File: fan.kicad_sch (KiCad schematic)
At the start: 10 parts, among them J6 Conn_01x04, U25 TMP1075NDRLR, U9 EMC2101

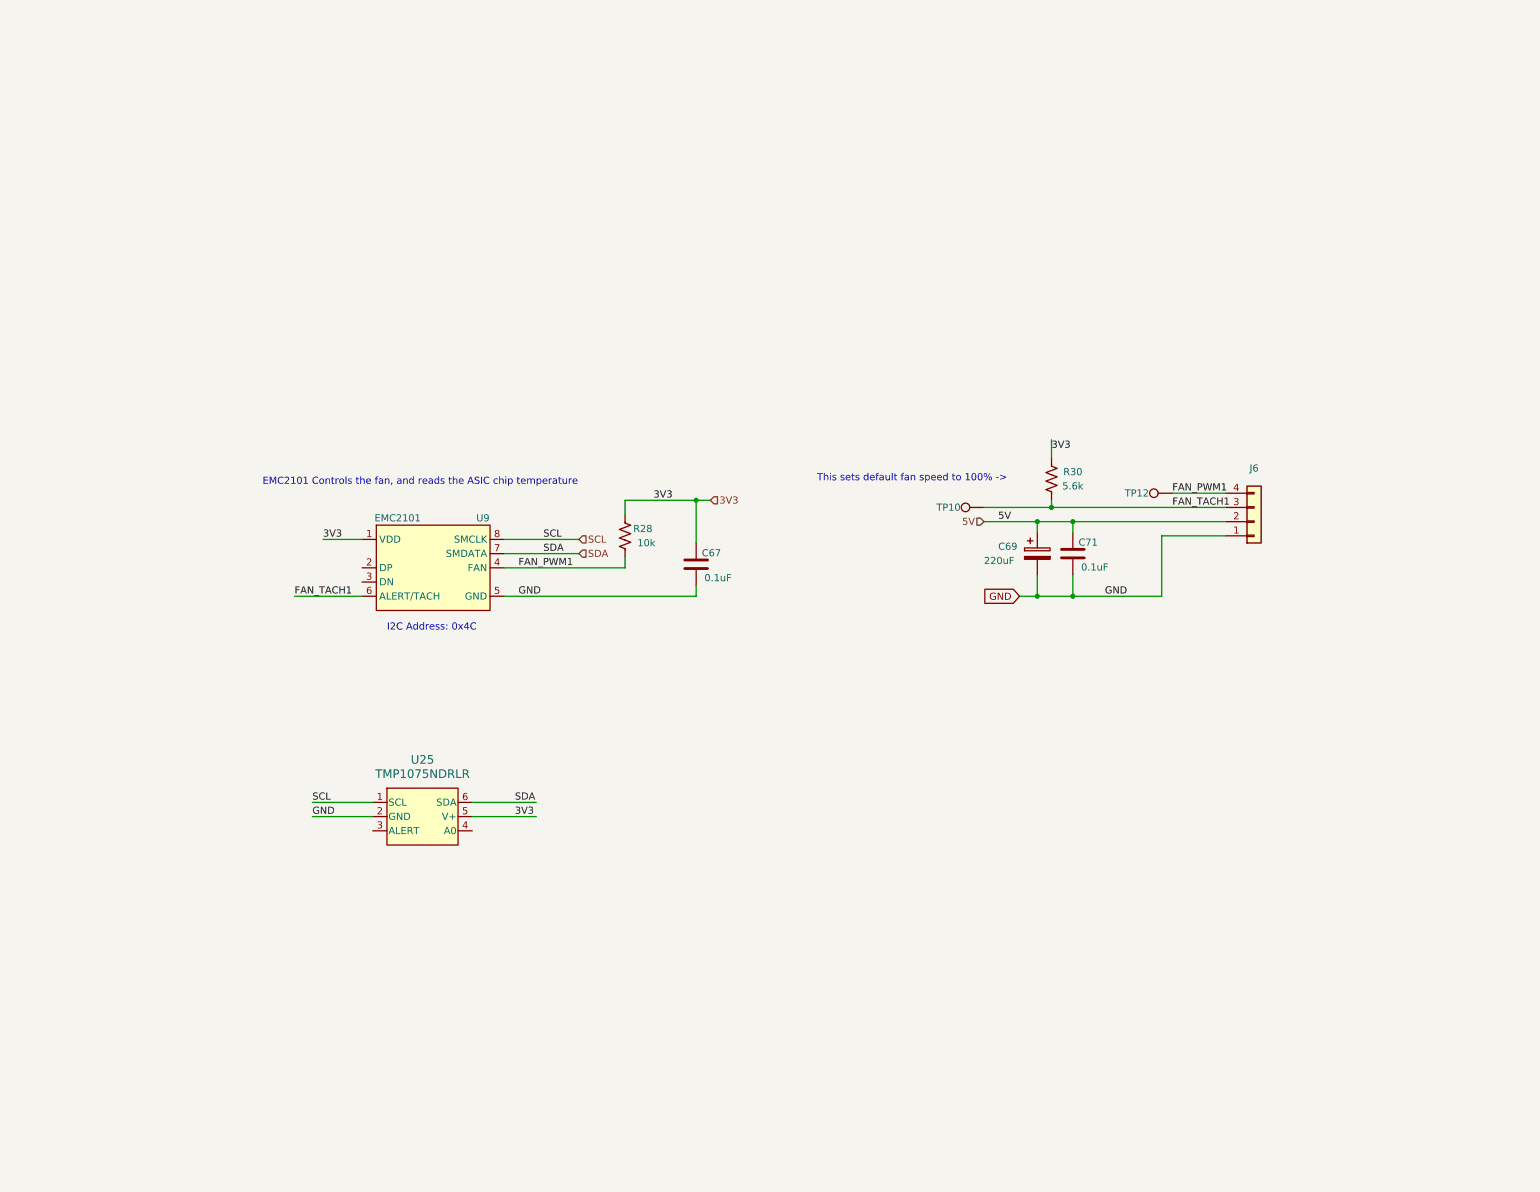
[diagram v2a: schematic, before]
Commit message: added EMC2302
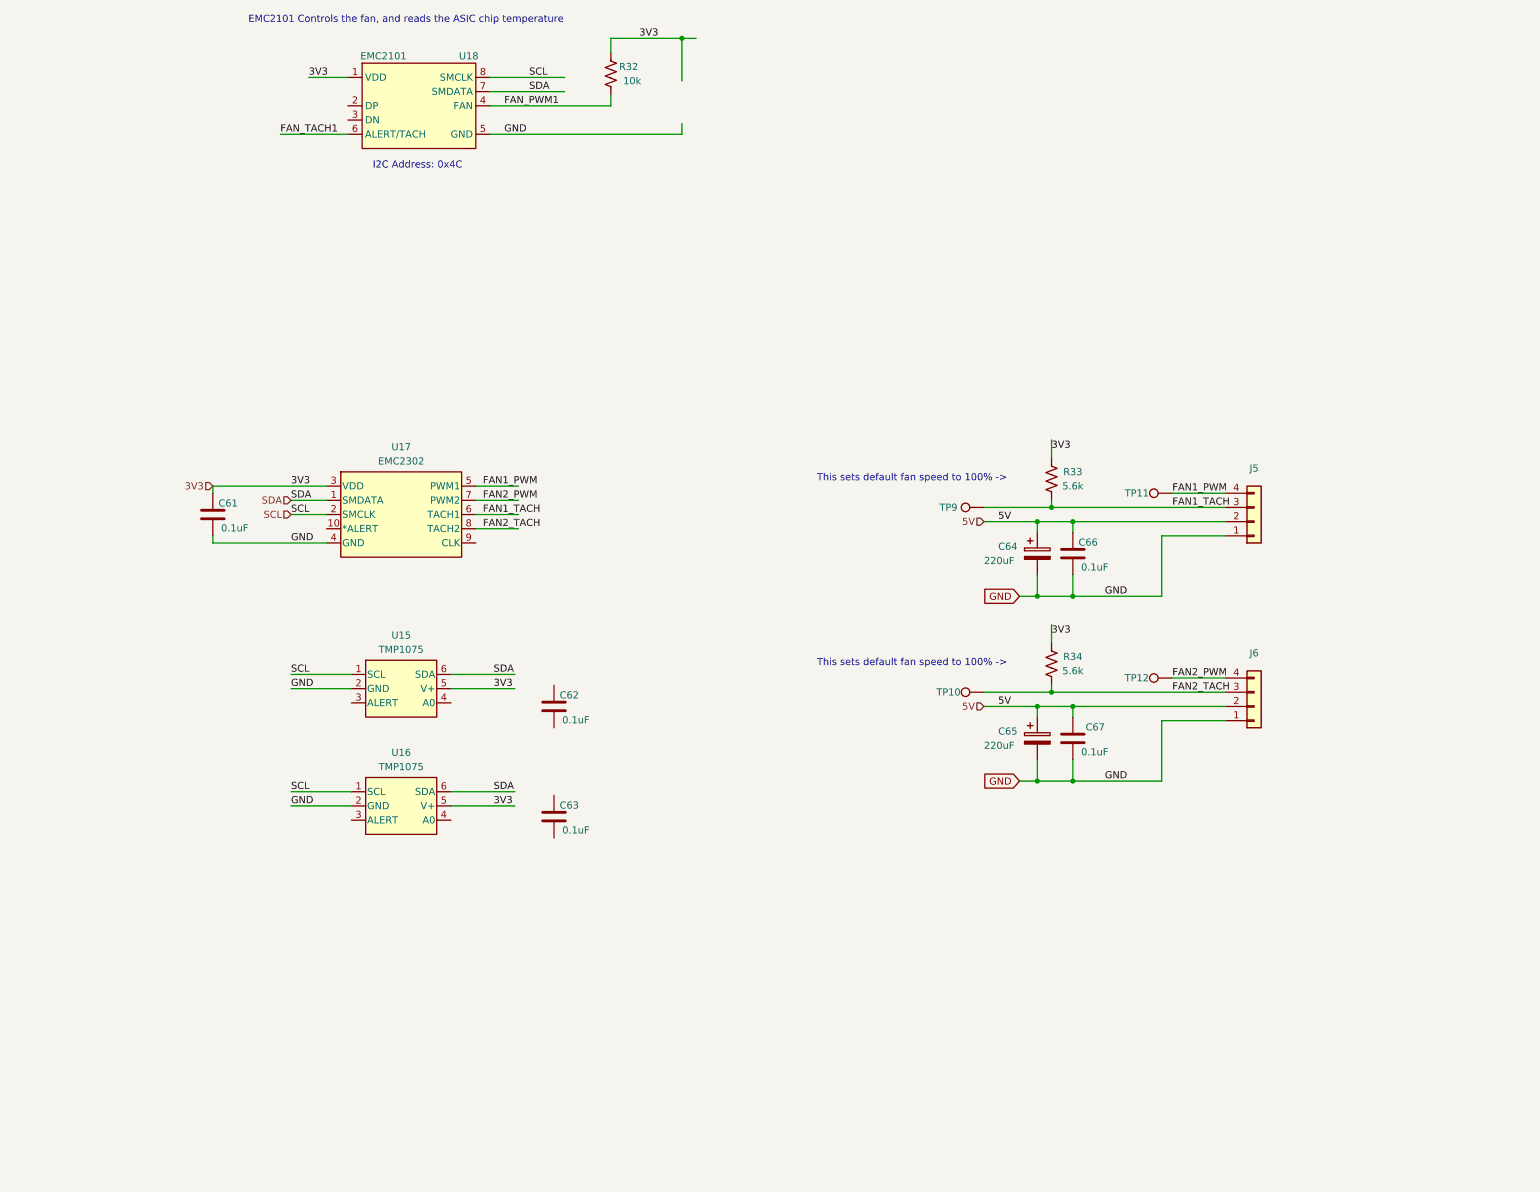
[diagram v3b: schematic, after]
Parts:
- added C62, C63, C67: 311-3342-1-ND, Capacitor_SMD:C_0402_1005Metric, symbol Device:C
- added C65: 220uF, Capacitor_SMD:CP_Elec_6.3x7.7, symbol Device:C_Polarized
- added J6: Conn_01x04, bitaxe:470531000, symbol Connector_Generic:Conn_01x04
- added R34: 5.6k, Resistor_SMD:R_0402_1005Metric, symbol Device:R_US
- added TP10, TP12: TestPoint, TestPoint:TestPoint_Pad_D1.5mm, symbol Connector:TestPoint
- added U16: TMP1075, bitaxe:SOT5X3-6_DRL_TEX, symbol bitaxe:TMP1075NDRLR
- added U17: EMC2302, MSOP10_MC_MCH, symbol bitaxe:EMC2302-2-AIZL-TR
- U15: renamed from U25; value TMP1075NDRLR -> TMP1075
- renumbered C67 to C61, C69 to C64, C71 to C66, J6 to J5, R28 to R32, R30 to R33, TP12 to TP11, TP10 to TP9, U9 to U18
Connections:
- net 3V3: now also R34.2, U16.5 (V+), U17.3 (VDD)
- net 5V: now also C65.1, C67.1, J6.2 (Pin_2)
- net FAN_PWM1: no longer J5.4 (Pin_4), TP11.1
- net FAN_TACH1: no longer J5.3 (Pin_3), R33.1, TP9.1
- net GND: now also C65.2, C67.2, J6.1 (Pin_1), U16.2 (GND), U17.4 (GND)
- net SCL: now also U16.1 (SCL), U17.2 (SMCLK)
- net SDA: now also U16.6 (SDA), U17.1 (SMDATA)
- new net FAN1_PWM: J5.4 (Pin_4), TP11.1, U17.5 (PWM1)
- new net FAN1_TACH: J5.3 (Pin_3), R33.1, TP9.1, U17.6 (TACH1)
- new net FAN2_PWM: J6.4 (Pin_4), TP12.1, U17.7 (PWM2)
- new net FAN2_TACH: J6.3 (Pin_3), R34.1, TP10.1, U17.8 (TACH2)
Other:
- moved on the sheet: C61, R32, U15, U18

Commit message: added DK and PARTNO for the fan controller and temp sensors
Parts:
- U15, U16: DK (none) -> 296-TMP1075NDRLRCT-ND; PARTNO (none) -> TMP1075NDRLR
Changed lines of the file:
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@@
       (effects (font (size 1.27 1.27) italic) hide)
     )
-    (property "Datasheet" "EMC2302-2-AIZL-TR" (at 90.805 68.58 0)
+    (property "Datasheet" "https://ww1.microchip.com/downloads/aemDocuments/documents/MSLD/ProductDocuments/DataSheets/EMC2301-2-3-5-Data-Sheet-DS20006532A.pdf" (at 90.805 68.58 0)
       (effects (font (size 1.27 1.27) italic) hide)
     )
@@
       (effects (font (size 1.27 1.27) italic) hide)
     )
+    (property "PARTNO" "TMP1075NDRLR" (at 71.12 104.14 0)
+      (effects (font (size 1.27 1.27)) hide)
+    )
+    (property "DK" "296-TMP1075NDRLRCT-ND" (at 71.12 104.14 0)
+      (effects (font (size 1.27 1.27)) hide)
+    )
     (pin "1")
     (pin "2")
@@
       (effects (font (size 1.27 1.27) italic) hide)
     )
-    (pin "1")
+    (property "DK" "296-TMP1075NDRLRCT-ND" (at 71.12 83.185 0)
+      (effects (font (size 1.27 1.27)) hide)
+    )
+    (property "PARTNO" "TMP1075NDRLR" (at 71.12 83.185 0)
+      (effects (font (size 1.27 1.27)) hide)
+    )
+    (pin "1")

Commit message: moved all custom symbols and footprints to the bitaxe library
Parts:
- U17: footprint MSOP10_MC_MCH -> Package_SO:MSOP-10_3x3mm_P0.5mm
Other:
- title: (none) -> bitaxeUltraHex
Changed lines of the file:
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@@
 (kicad_sch (version 20230121) (generator eeschema)
   (paper "A")
+  (title_block
+    (title "bitaxeUltraHex")
+    (date "2023-06-11")
+    (rev "1")
+  )
   (junction (at 205.105 99.695) (diameter 0) (color 0 0 0 0)
   )
@@
       (effects (font (size 1.27 1.27)))
     )
-    (property "Footprint" "MSOP10_MC_MCH" (at 88.265 66.04 0)
+    (property "Footprint" "Package_SO:MSOP-10_3x3mm_P0.5mm" (at 88.265 66.04 0)
       (effects (font (size 1.27 1.27) italic) hide)
     )
@@
     )
   )
-  (symbol (lib_id "bitaxe:TMP1075NDRLR") (at 71.12 83.185 0) (unit 1)
+  (symbol (lib_name "TMP1075NDRLR_1") (lib_id "bitaxe:TMP1075NDRLR") (at 71.12 83.185 0) (unit 1)
     (in_bom yes) (on_board yes) (dnp no) (fields_autoplaced)
     (property "Reference" "U15" (at 91.44 73.66 0)

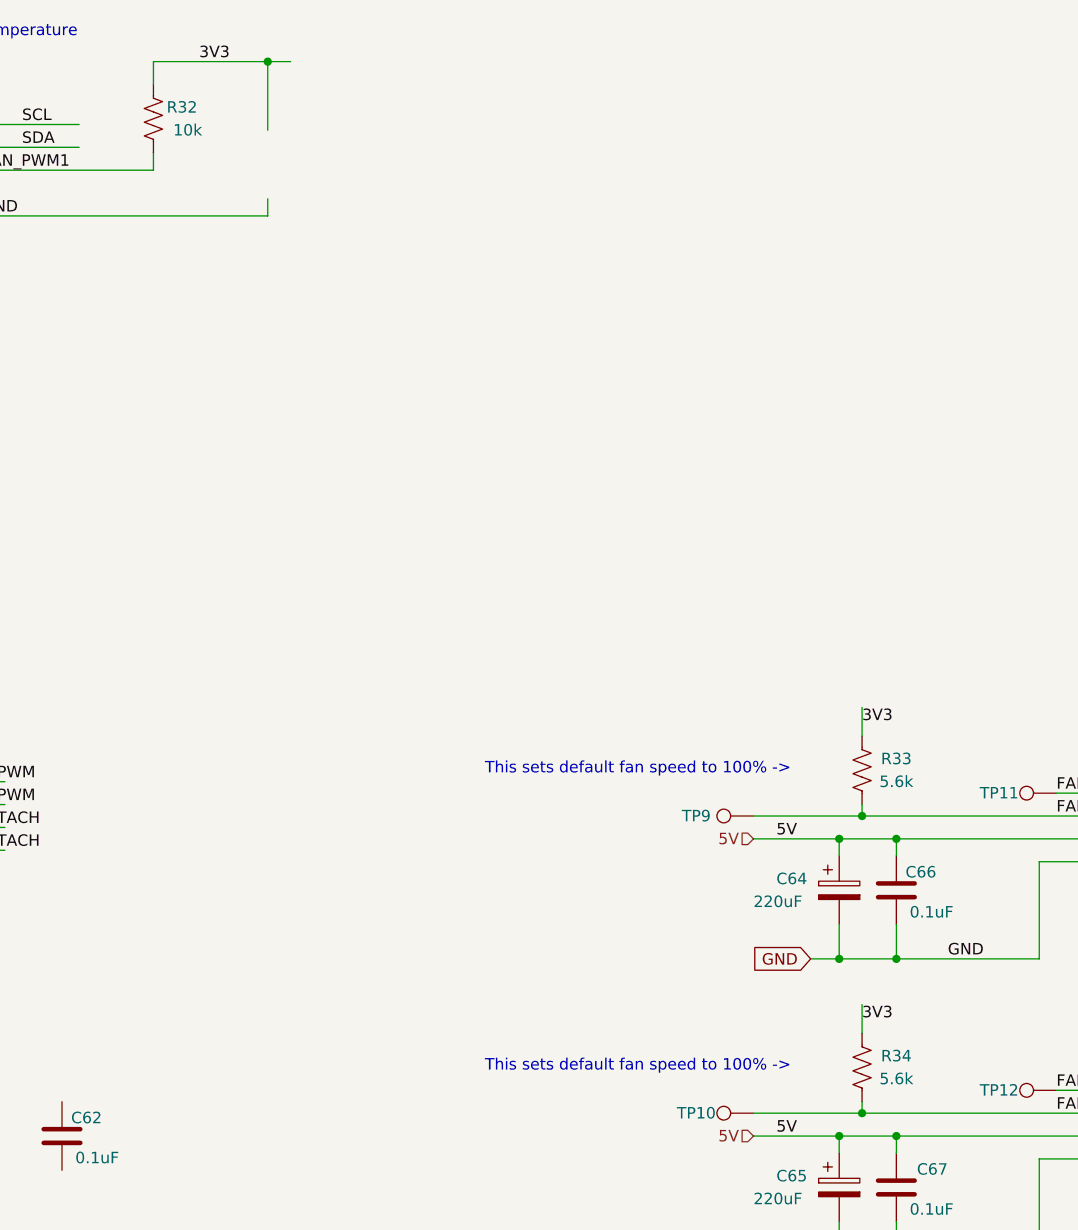
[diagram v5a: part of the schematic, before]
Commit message: switch voltage reference regulators to ADP170, reannotate
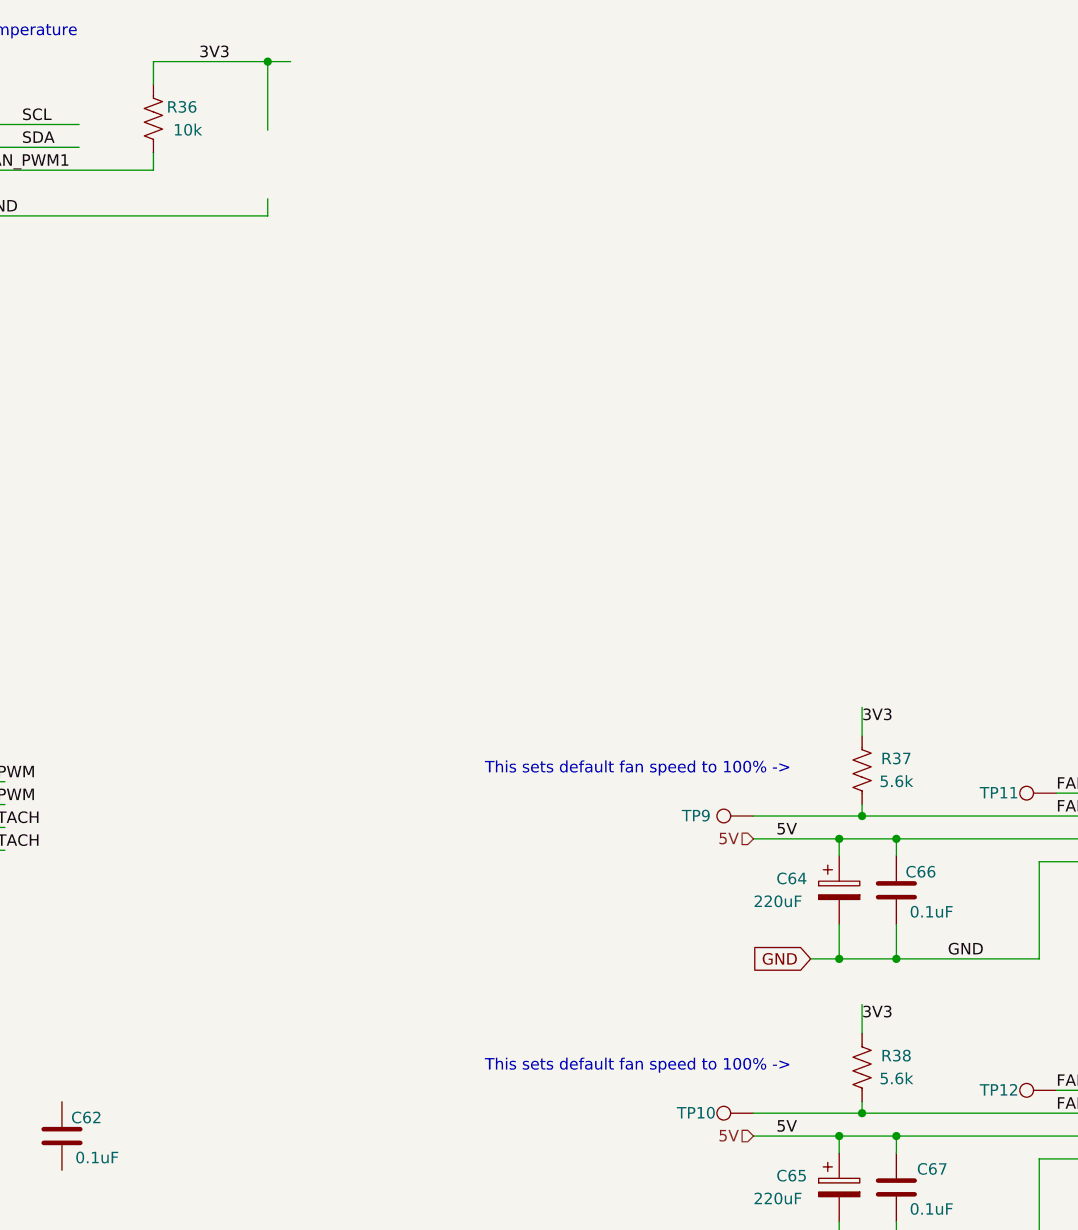
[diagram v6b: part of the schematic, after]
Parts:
- renumbered R32 to R36, R33 to R37, R34 to R38
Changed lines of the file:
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@@
   (symbol (lib_id "Device:R_US") (at 207.645 45.72 180) (unit 1)
     (in_bom yes) (on_board yes) (dnp no)
-    (property "Reference" "R33" (at 211.455 44.45 0)
+    (property "Reference" "R37" (at 211.455 44.45 0)
       (effects (font (size 1.27 1.27)))
     )
@@
       (project "bitaxeUltraHex"
         (path "/e63e39d7-6ac0-4ffd-8aa3-1841a4541b55/8e8832ea-6bf1-49d2-b3a5-32a207f555d2"
-          (reference "R33") (unit 1)
+          (reference "R37") (unit 1)
         )
       )
@@
   (symbol (lib_id "Device:R_US") (at 207.645 78.74 180) (unit 1)
     (in_bom yes) (on_board yes) (dnp no)
-    (property "Reference" "R34" (at 211.455 77.47 0)
+    (property "Reference" "R38" (at 211.455 77.47 0)
       (effects (font (size 1.27 1.27)))
     )
@@
       (project "bitaxeUltraHex"
         (path "/e63e39d7-6ac0-4ffd-8aa3-1841a4541b55/8e8832ea-6bf1-49d2-b3a5-32a207f555d2"
-          (reference "R34") (unit 1)
+          (reference "R38") (unit 1)
         )
       )
@@
   (symbol (lib_id "Device:R_US") (at 128.905 -26.67 180) (unit 1)
     (in_bom yes) (on_board yes) (dnp no)
-    (property "Reference" "R32" (at 132.08 -27.94 0)
+    (property "Reference" "R36" (at 132.08 -27.94 0)
       (effects (font (size 1.27 1.27)))
     )
@@
       (project "bitaxeUltraHex"
         (path "/e63e39d7-6ac0-4ffd-8aa3-1841a4541b55/8e8832ea-6bf1-49d2-b3a5-32a207f555d2"
-          (reference "R32") (unit 1)
-        )
-      )
+          (reference "R36") (unit 1)
+        )
+      )
